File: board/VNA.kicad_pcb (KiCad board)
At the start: 2 copper layers, 100 x 100 mm, 144 parts, among them J1 Conn_02x07_Odd_Even, J10 Conn_01x01, J11 Conn_01x01, J12 Conn_01x01, J13 Barrel_Jack, J14 Conn_01x02, J15 Conn_02x05_Odd_Even, J17 Conn_01x04, J18 Conn_01x01, J19 Conn_01x01, J2 Conn_Coaxial, J20 Conn_01x01, J21 Conn_01x01, J22 Conn_01x02, J3 Conn_01x01, J4 Conn_01x01, J5 Conn_01x01, J6 Conn_01x01, J7 Conn_01x01, J8 Conn_01x01, J9 Conn_Coaxial, Q1 SS9018, U1 SI5351A, U10 SI5351A, U2 LM339, U3 SA612, U4 SA612, U5 SA612, U6 LM358, U7 LM358, U8 LM1117-3.3, U9 LM7805_TO220, Y1 27 MHz

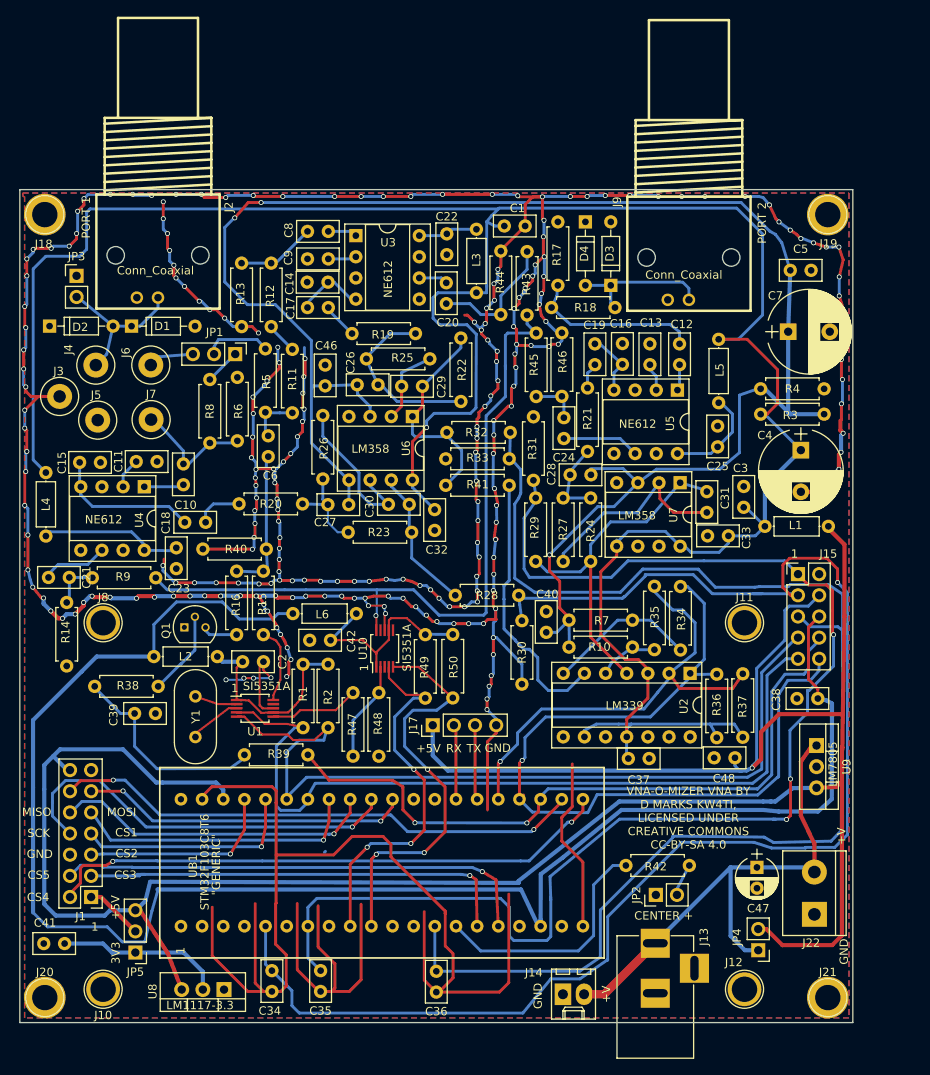
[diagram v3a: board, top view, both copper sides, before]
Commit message: Added SD card slot, reorganized pins
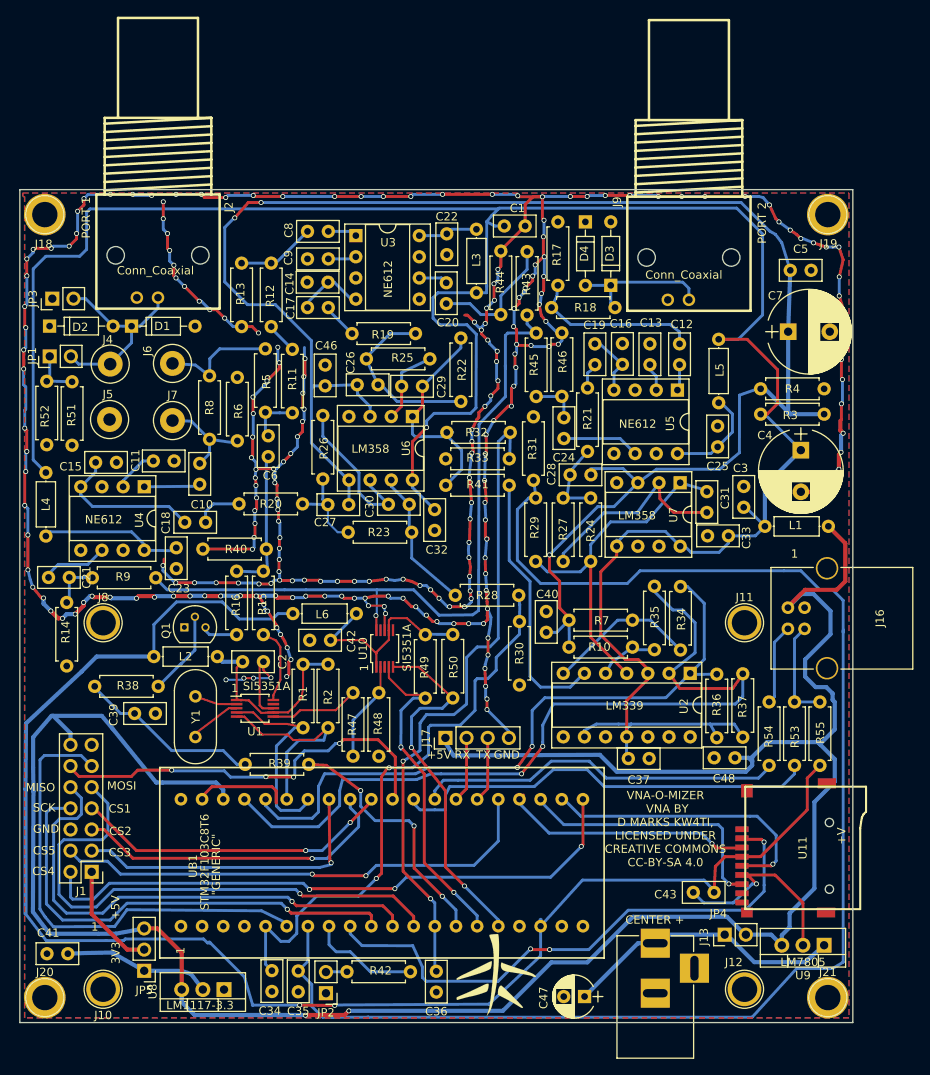
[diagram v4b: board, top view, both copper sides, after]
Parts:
- removed C38: 100 nF, Capacitors_THT:C_Disc_D5.0mm_W2.5mm_P2.50mm
- removed J14: Conn_01x02, Connectors_Molex:Molex_KK-6410-02_02x2.54mm_Straight
- removed J15: Conn_02x05_Odd_Even, Pin_Headers:Pin_Header_Straight_2x05_Pitch2.54mm
- removed J22: Conn_01x02, Connectors_Terminal_Blocks:TerminalBlock_bornier-2_P5.08mm
- removed J3: Conn_01x01, Connectors:1pin
- added C43: 100 nF, Capacitors_THT:C_Disc_D5.0mm_W2.5mm_P2.50mm, F.Cu at (133.3, 134.4)
- added G***: LOGO, VNA:VNAOMizer, F.Cu at (107.2, 144.3)
- added J16: USB_B, Connectors:USB_B, F.Cu at (142.2, 100.2)
- added R51: 100R, Resistors_THT:R_Axial_DIN0207_L6.3mm_D2.5mm_P7.62mm_Horizontal, F.Cu at (56.3, 80.7)
- added R52: 100R, Resistors_THT:R_Axial_DIN0207_L6.3mm_D2.5mm_P7.62mm_Horizontal, F.Cu at (53.2, 80.6)
- added R53: 22R, Resistors_THT:R_Axial_DIN0207_L6.3mm_D2.5mm_P7.62mm_Horizontal, F.Cu at (143.0, 119.1)
- added R54: 22R, Resistors_THT:R_Axial_DIN0207_L6.3mm_D2.5mm_P7.62mm_Horizontal, F.Cu at (140.0, 119.1)
- added R55: NC, Resistors_THT:R_Axial_DIN0207_L6.3mm_D2.5mm_P7.62mm_Horizontal, F.Cu at (146.1, 119.1)
- added U11: MicroSD_SPI_CD, VNA:GCT-MEM2055-00-190-01-A, F.Cu at (135.9, 129.0)
- JP1: value Jumper_NC_Dual -> Jumper_NC_Small; footprint Pin_Headers:Pin_Header_Straight_1x03_Pitch2.54mm -> Pin_Headers:Pin_Header_Straight_1x02_Pitch2.54mm
- moved R42 43.0 mm to (89.3, 143.9), turned to 0 degrees
- moved JP2 41.3 mm to (86.8, 146.5), turned to 180 degrees
- moved C47 25.9 mm to (117.8, 146.9), turned to 180 degrees
- moved U9 24.0 mm to (146.6, 140.7), turned to 180 degrees
- moved JP1 22.3 mm to (53.6, 70.0), turned to 90 degrees
- moved JP4 4.44 mm to (134.6, 139.4), turned to 90 degrees
- moved JP3 4.00 mm to (53.9, 63.1), turned to 90 degrees
- moved J1 3.03 mm to (58.6, 131.9)
- moved C35 2.68 mm to (83.4, 143.8)
- moved J6 2.61 mm to (68.3, 70.9)
- moved J7 2.57 mm to (68.3, 77.7)
- moved JP5 2.43 mm to (64.9, 143.8)
- moved J17 2.16 mm to (101.1, 115.8)
- moved C11 2.05 mm to (66.0, 82.6)
- moved C10 1.96 mm to (71.6, 85.4)
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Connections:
- J1 pad 10: Net-(J1-Pad10) -> MISO1
- J1 pad 11: Net-(J1-Pad11) -> PA1
- J1 pad 12: Net-(J1-Pad12) -> PA15
- J1 pad 3: PB10 -> PB5
- J1 pad 4: PB11 -> PA8
- J1 pad 5: Net-(J1-Pad5) -> PB4
- J1 pad 7: Net-(J1-Pad7) -> PB3
- J1 pad 8: Net-(J1-Pad8) -> SCK1
- J1 pad 9: Net-(J1-Pad9) -> MOSI1
- JP1 pad 2: Net-(JP1-Pad2) -> Net-(D1-Pad1)
- R42 pad 2: Net-(R42-Pad2) -> NODISPLAY
- R5 pad 1: Net-(JP1-Pad2) -> Net-(J6-Pad1)
- R8 pad 2: Net-(JP1-Pad1) -> Net-(J6-Pad1)
- U8 pad 1: (no net) -> GND
- UB1 pad 11: (no net) -> PA1
- UB1 pad 13: (no net) -> NODISPLAY
- UB1 pad 14: SCL2 -> SD_CS
- UB1 pad 15: SDA2 -> SCK1
- UB1 pad 16: (no net) -> MISO1
- UB1 pad 17: (no net) -> MOSI1
- UB1 pad 19: Net-(R42-Pad2) -> ATTEN
- UB1 pad 21: PB10 -> SCL2
- UB1 pad 22: PB11 -> SDA2
- UB1 pad 26: Net-(J1-Pad12) -> Net-(U11-Pad5)
- UB1 pad 27: ATTEN -> Net-(U11-Pad7)
- UB1 pad 28: SYNCSAMPLE -> Net-(U11-Pad3)
- UB1 pad 29: SYNCSAMPLE2 -> PA8
- UB1 pad 32: (no net) -> Net-(R54-Pad1)
- UB1 pad 33: (no net) -> Net-(R53-Pad1)
- UB1 pad 38: Net-(J1-Pad11) -> PA15
- UB1 pad 39: Net-(J1-Pad8) -> PB3
- UB1 pad 40: Net-(J1-Pad10) -> PB4
- UB1 pad 41: Net-(J1-Pad9) -> PB5
- UB1 pad 45: Net-(J1-Pad7) -> SYNCSAMPLE
- UB1 pad 46: Net-(J1-Pad5) -> SYNCSAMPLE2
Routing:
- net GND: track 760.9 -> 585.0 mm, vias 232 -> 231
- net DEMODCUR: track 175.3 -> 70.3 mm, vias 1 -> 2
- net DEMODVOLT: track 161.4 -> 79.1 mm, vias 0 -> 2
- net SDA: track 101.2 -> 25.3 mm
- net SCL: track 98.3 -> 25.6 mm
- net SD_CS: track 0.00 -> 67.6 mm, vias 0 -> 3
- net MOSI1: track 0.00 -> 65.6 mm, vias 0 -> 1
- net Net-(J1-Pad12): track 63.9 -> 0.00 mm, vias 2 -> 0
- net MISO1: track 0.00 -> 61.1 mm, vias 0 -> 1
- net PA8: track 0.00 -> 59.4 mm, vias 0 -> 2
- net PB11: track 57.7 -> 0.00 mm, vias 1 -> 0
- net PA1: track 0.00 -> 57.3 mm
- net SCK1: track 0.00 -> 56.6 mm, vias 0 -> 1
- net ATTEN: track 84.2 -> 30.6 mm, vias 2 -> 3
- net PB10: track 53.0 -> 0.00 mm, vias 1 -> 0
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
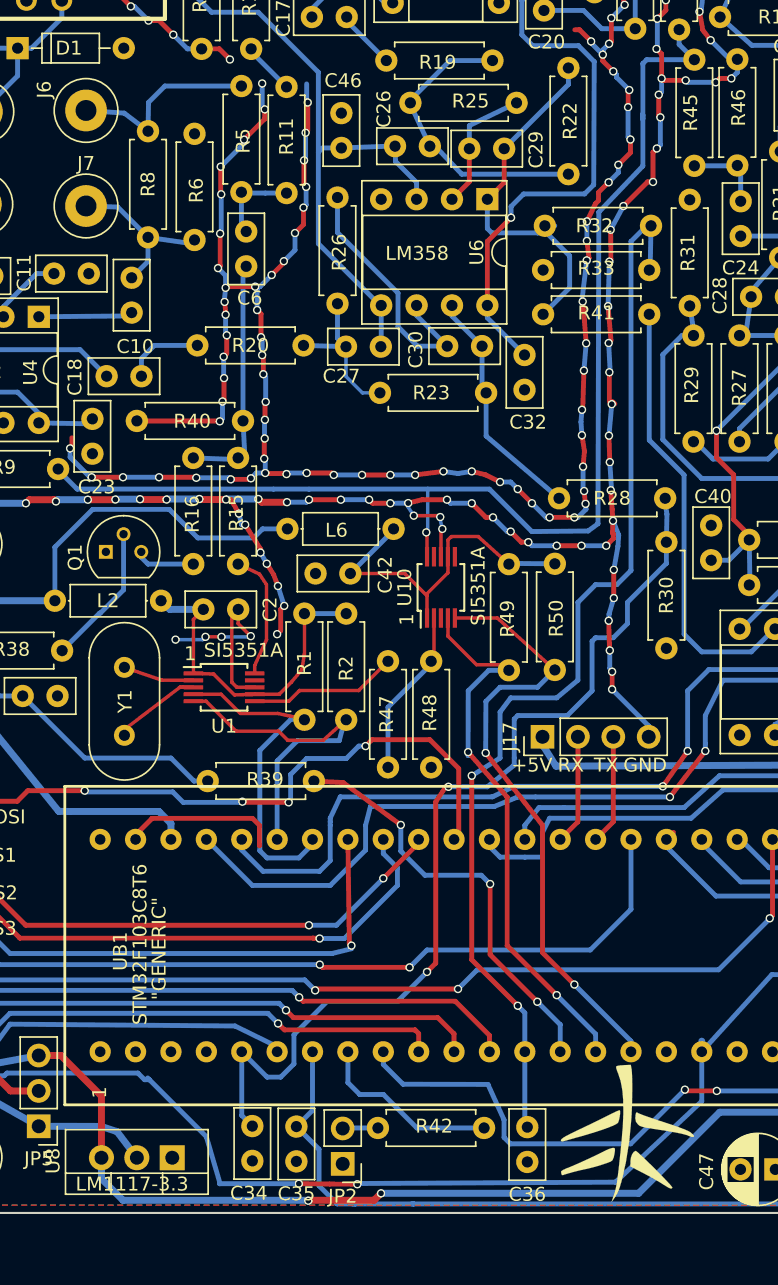
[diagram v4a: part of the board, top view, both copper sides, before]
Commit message: Adds SD card support, which is mandatory.  Also changed firmware for new pinouts.
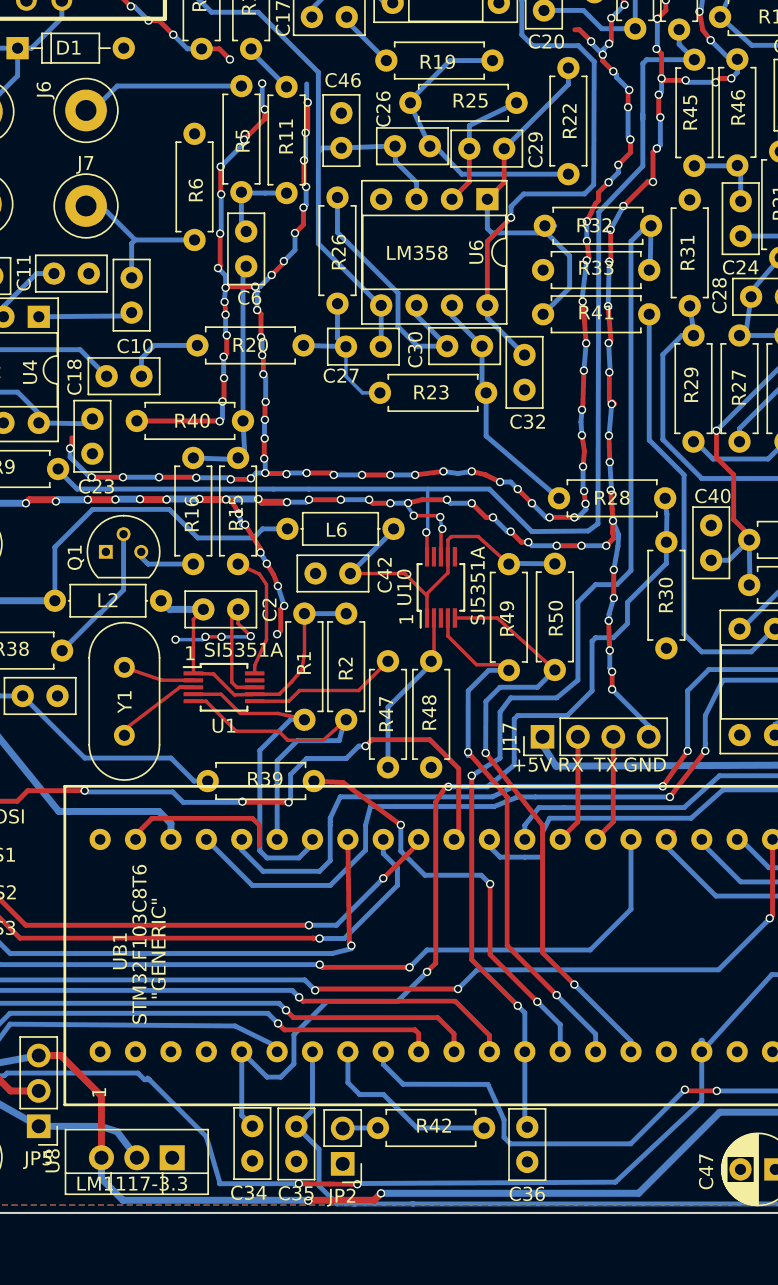
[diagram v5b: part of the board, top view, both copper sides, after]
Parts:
- removed G***: LOGO, VNA:VNAOMizer
- removed R8: 51R, Resistors_THT:R_Axial_DIN0207_L6.3mm_D2.5mm_P7.62mm_Horizontal
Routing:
- net Net-(J6-Pad1): track 14.1 -> 11.9 mm
- net SAMPCUR: track 13.3 -> 12.4 mm

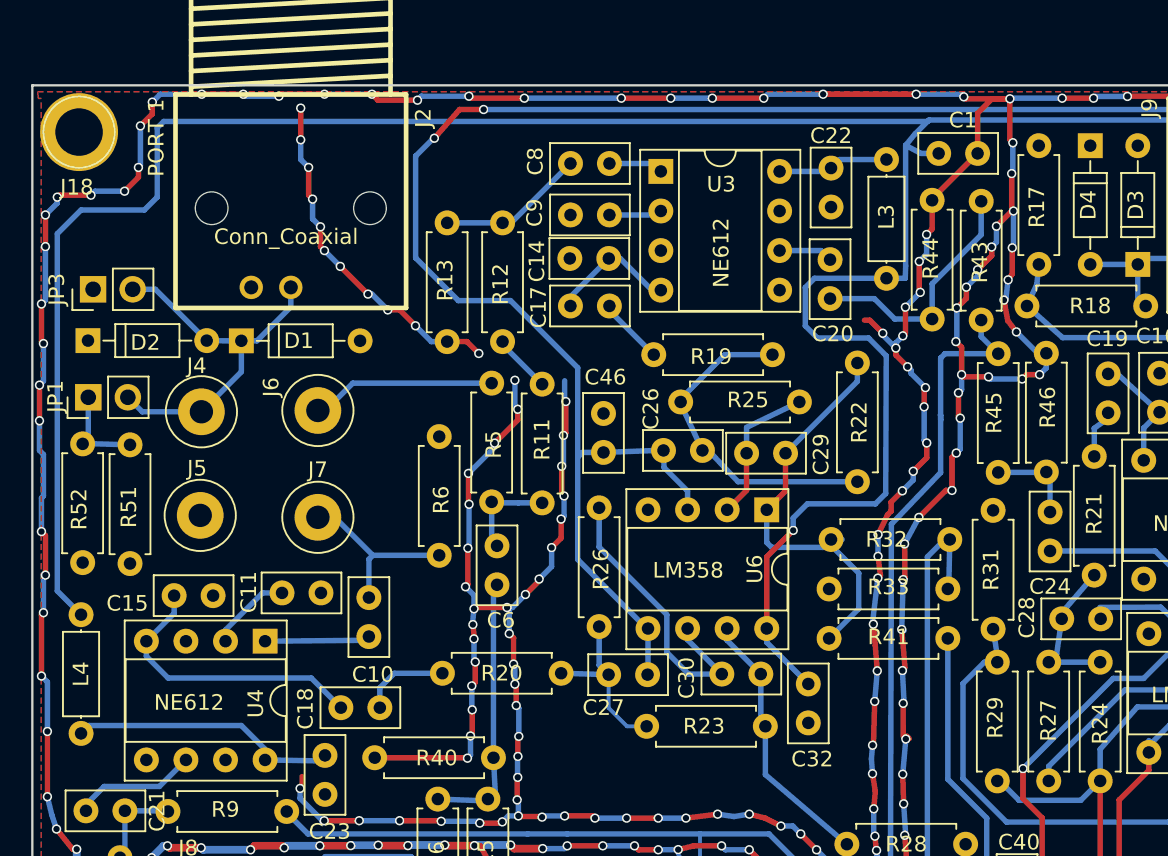
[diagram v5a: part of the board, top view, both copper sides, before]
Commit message: Changed to resistive bridge
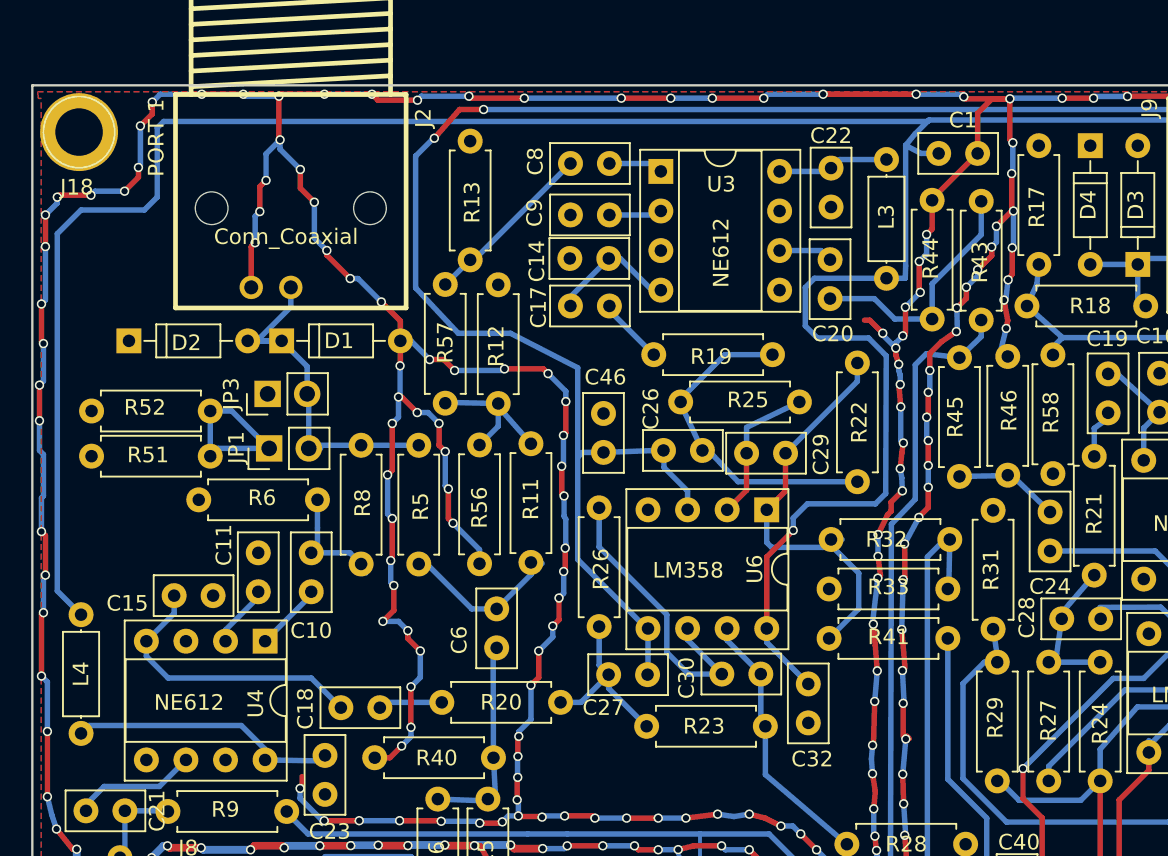
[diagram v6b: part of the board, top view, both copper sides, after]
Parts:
- removed J4, J5, J6, J7: Conn_01x01, Connectors:1pin
- added R56: 100R, Resistors_THT:R_Axial_DIN0207_L6.3mm_D2.5mm_P7.62mm_Horizontal, F.Cu at (78.7, 80.7)
- added R57: 120R, Resistors_THT:R_Axial_DIN0207_L6.3mm_D2.5mm_P7.62mm_Horizontal, F.Cu at (76.5, 70.4)
- added R58: 22R, Resistors_THT:R_Axial_DIN0207_L6.3mm_D2.5mm_P7.62mm_Horizontal, F.Cu at (115.5, 67.3)
- added R8: 120R, Resistors_THT:R_Axial_DIN0207_L6.3mm_D2.5mm_P7.62mm_Horizontal, F.Cu at (71.1, 73.1)
- R11, R5: value 220R -> 47R
- R12: value 51R -> 100R
- R13, R6: value 5R1 -> 4R7
- R43, R45, R9: value 1.5k -> 1k5
- moved JP3 13.1 mm to (65.1, 69.8)
- moved JP1 12.1 mm to (65.2, 73.3)
- moved R52 9.75 mm to (53.8, 70.9), turned to 0 degrees
- moved R6 8.59 mm to (68.3, 76.6), turned to 180 degrees
- moved R51 7.32 mm to (53.8, 73.8), turned to 0 degrees
- moved R5 6.15 mm to (74.8, 73.1)
- moved C10 4.69 mm to (67.9, 82.5)
- moved C6 4.05 mm to (79.8, 86.1)
- moved R12 3.98 mm to (79.9, 62.8)
- moved R11 3.89 mm to (82.0, 73.0)
- moved R13 2.80 mm to (78.1, 61.2), turned to 90 degrees
- moved D2 2.63 mm to (56.2, 66.4)
- moved D1 2.59 mm to (66.0, 66.4)
- moved R45 2.50 mm to (109.5, 75.1)
- moved R46 2.48 mm to (112.6, 67.4)
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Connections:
- net SAMPCUR renamed SAMPPORT
- R12 pad 1: SAMPVOLT -> GND
- R5 pad 1: Net-(J6-Pad1) -> Net-(D1-Pad1)
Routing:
- net GND: track 585.0 -> 603.6 mm
- net Net-(J6-Pad1): track 11.9 -> 0.00 mm
- net Net-(R11-Pad1): track 3.78 -> 9.95 mm
- net CLK0: track 6.23 -> 12.1 mm
- net Net-(JP1-Pad1): track 6.26 -> 11.7 mm
- net SAMPPORT: track 12.4 -> 8.14 mm
- net Net-(C6-Pad1): track 17.3 -> 13.3 mm
- net Net-(C10-Pad1): track 6.76 -> 4.40 mm
- net SAMPVOLT: track 9.49 -> 11.3 mm
- net Net-(R43-Pad2): track 86.8 -> 85.1 mm
- net Net-(C18-Pad1): track 5.86 -> 4.30 mm
- net SAMPCUR2: track 20.7 -> 22.1 mm
- net Net-(C11-Pad1): track 5.33 -> 4.37 mm
- net CLK1C: track 5.82 -> 6.69 mm
- net 2V0: track 210.6 -> 211.4 mm
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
